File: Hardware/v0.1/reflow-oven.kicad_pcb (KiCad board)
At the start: 2 copper layers, 43 x 72 mm, 2 parts, among them U1 WeAct_MiniF4

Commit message: Finished schematics
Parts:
- added BZ1: HNB09A03, _AKL_Speaker:HNB09A03, B.Cu at (11.2, -23.0)
- added C1: 100n, Capacitor_SMD:C_0603_1608Metric, B.Cu at (0.10, -23.3)
- added C2: 10n, Capacitor_SMD:C_0603_1608Metric, B.Cu at (0.10, -25.8)
- added D1: MBR120VLSFT3G, _AKL_Diode:SOD-123FL, F.Cu at (-3.10, -63.0)
- added D2: MBR120VLSFT3G, _AKL_Diode:SOD-123FL, F.Cu at (-3.10, -59.9)
- added FB1: Ferrite_Bead, Inductor_SMD:L_0603_1608Metric, B.Cu at (4.11, -23.3)
- added FB2: Ferrite_Bead, Inductor_SMD:L_0603_1608Metric, B.Cu at (4.11, -25.8)
- added J1: WJ124-3.81-2P, _AKL_Connector:WJ124-3.81-2P, B.Cu at (-14.9, -22.6)
- added J2: WJ124-3.81-2P, _AKL_Connector:WJ124-3.81-2P, B.Cu at (-14.9, -15.0)
- added J3: WJ124-3.81-2P, _AKL_Connector:WJ124-3.81-2P, B.Cu at (-14.9, -7.37)
- added J4: WJ124-3.81-2P, _AKL_Connector:WJ124-3.81-2P, B.Cu at (-14.9, 0.25)
- added Q1: FDN327N, Package_TO_SOT_SMD:SOT-23, F.Cu at (1.94, -62.2)
- added Q2: FDN327N, Package_TO_SOT_SMD:SOT-23, F.Cu at (1.94, -57.7)
- added R1: 10K, Resistor_SMD:R_0603_1608Metric, F.Cu at (-3.96, -57.2)
- added R2: 10K, Resistor_SMD:R_0603_1608Metric, F.Cu at (6.17, -63.3)
- added R3: 10K, Resistor_SMD:R_0603_1608Metric, F.Cu at (6.17, -60.7)
- added R4: 10K, Resistor_SMD:R_0603_1608Metric, F.Cu at (6.17, -58.2)
- added R5: 10K, Resistor_SMD:R_0603_1608Metric, F.Cu at (6.17, -55.7)
- added SW1: TS-1095-A13B3-D1, Button_Switch_THT:SW_PUSH_6mm_H9.5mm, F.Cu at (-15.0, 34.0)
- added SW2: TS-1095-A13B3-D1, Button_Switch_THT:SW_PUSH_6mm_H9.5mm, F.Cu at (-2.25, 34.0)
- added SW3: TS-1095-A13B3-D1, Button_Switch_THT:SW_PUSH_6mm_H9.5mm, F.Cu at (10.5, 34.0)
- added U2: MAX31855KASA+T, Package_SO:SOIC-8_3.9x4.9mm_P1.27mm, B.Cu at (-6.77, -23.5)
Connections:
- DS1 pad 1: Net-(DS1-Pad1) -> /BL
- DS1 pad 2: Net-(DS1-Pad2) -> /RST
- DS1 pad 3: Net-(DS1-Pad3) -> /DC
- DS1 pad 4: Net-(DS1-Pad4) -> /CS1
- DS1 pad 5: Net-(DS1-Pad5) -> /SCK1
- DS1 pad 6: Net-(DS1-Pad6) -> /MOSI1
- DS1 pad 7: Net-(DS1-Pad7) -> GND
- DS1 pad 8: Net-(DS1-Pad8) -> /3V3
- U1 pad 1: Net-(U1-Pad1) -> /CS2
- U1 pad 10: Net-(U1-Pad10) -> (no net)
- U1 pad 11: Net-(U1-Pad11) -> (no net)
- U1 pad 12: Net-(U1-Pad12) -> (no net)
- U1 pad 13: Net-(U1-Pad13) -> /OUT1
- U1 pad 14: Net-(U1-Pad14) -> /OUT2
- U1 pad 15: Net-(U1-Pad15) -> (no net)
- U1 pad 16: Net-(U1-Pad16) -> (no net)
- U1 pad 17: Net-(U1-Pad17) -> (no net)
- U1 pad 18: Net-(U1-Pad18) -> /5V
- U1 pad 19: Net-(U1-Pad19) -> GND
- U1 pad 2: Net-(U1-Pad2) -> /SCK2
- U1 pad 20: Net-(U1-Pad20) -> /3V3
- U1 pad 21: Net-(U1-Pad21) -> (no net)
- U1 pad 22: Net-(U1-Pad22) -> (no net)
- U1 pad 23: Net-(U1-Pad23) -> (no net)
- U1 pad 24: Net-(U1-Pad24) -> (no net)
- U1 pad 25: Net-(U1-Pad25) -> (no net)
- U1 pad 26: Net-(U1-Pad26) -> (no net)
- U1 pad 27: Net-(U1-Pad27) -> /BUZZER
- U1 pad 28: Net-(U1-Pad28) -> /DC
- U1 pad 29: Net-(U1-Pad29) -> /RST
- U1 pad 3: Net-(U1-Pad3) -> /MISO2
- U1 pad 30: Net-(U1-Pad30) -> /CS1
- U1 pad 31: Net-(U1-Pad31) -> /SCK1
- U1 pad 32: Net-(U1-Pad32) -> /BL
- U1 pad 33: Net-(U1-Pad33) -> /MOSI1
- U1 pad 34: Net-(U1-Pad34) -> /BTN_C
- U1 pad 35: Net-(U1-Pad35) -> /BTN_B
- U1 pad 36: Net-(U1-Pad36) -> (no net)
- U1 pad 37: Net-(U1-Pad37) -> /BTN_A
- U1 pad 38: Net-(U1-Pad38) -> /3V3
- U1 pad 39: Net-(U1-Pad39) -> GND
- U1 pad 4: Net-(U1-Pad4) -> (no net)
- U1 pad 40: Net-(U1-Pad40) -> /5V
- U1 pad 5: Net-(U1-Pad5) -> (no net)
- U1 pad 6: Net-(U1-Pad6) -> (no net)
- U1 pad 7: Net-(U1-Pad7) -> (no net)
- U1 pad 8: Net-(U1-Pad8) -> (no net)
- U1 pad 9: Net-(U1-Pad9) -> (no net)

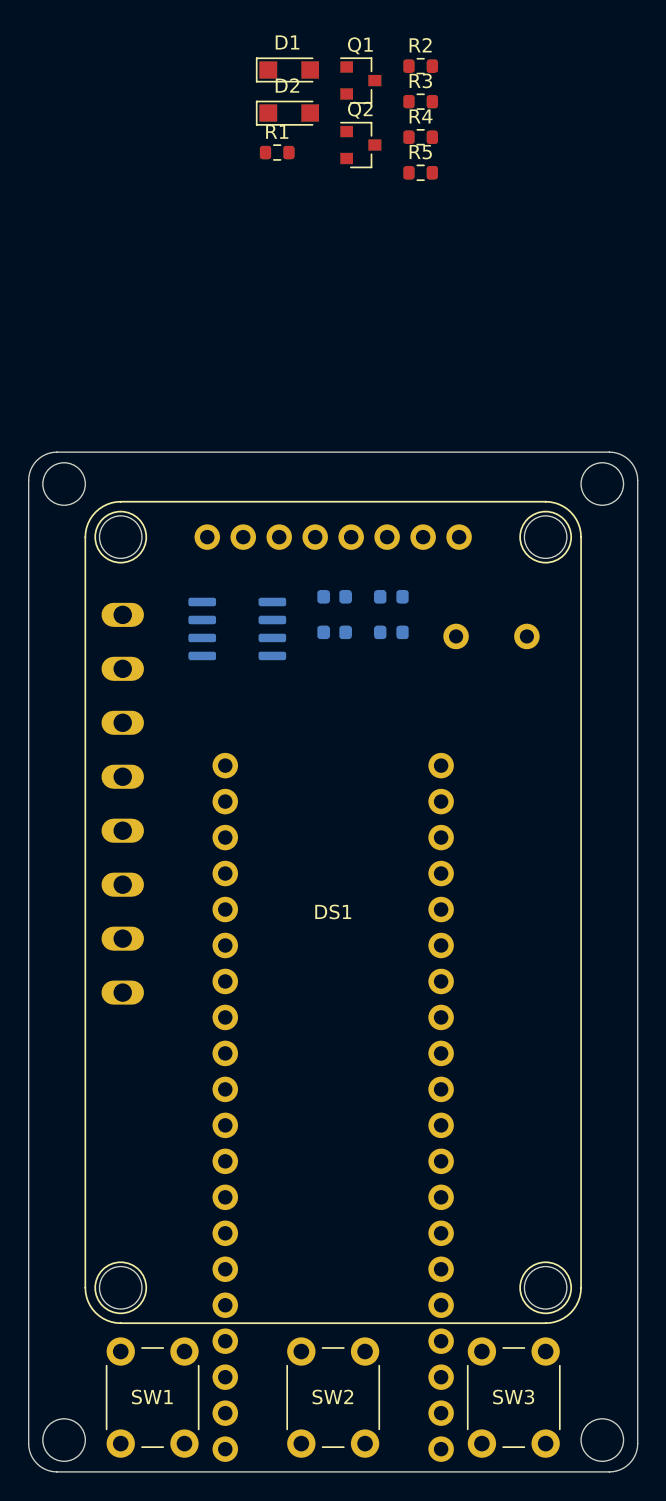
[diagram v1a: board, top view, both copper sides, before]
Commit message: Finished PCB layout
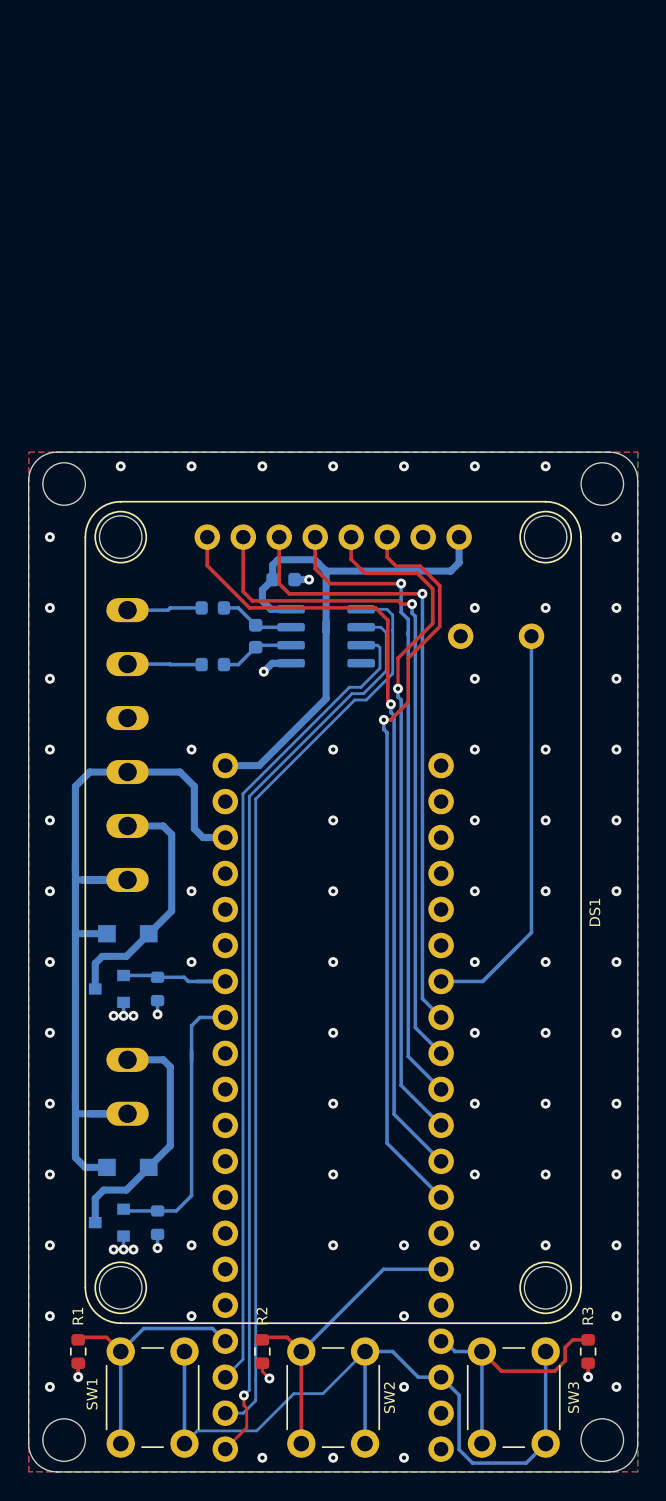
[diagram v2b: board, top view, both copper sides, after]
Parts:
- added REF**: OSHW-Logo_5.7x6mm_SilkScreen, Symbol:OSHW-Logo_5.7x6mm_SilkScreen, B.Cu at (15.5, -10.0)
- D1, D2, Q1, Q2, R4, R5: moved to B.Cu
- moved R2 91.4 mm to (-5.00, 27.5), turned to 270 degrees
- moved R3 89.0 mm to (18.0, 27.5), turned to 270 degrees
- moved R1 85.8 mm to (-18.0, 27.5), turned to 270 degrees
- moved Q2 78.1 mm to (-15.8, 18.4), turned to 180 degrees
- moved R5 76.4 mm to (-12.4, 18.4), turned to 270 degrees
- moved D2 75.3 mm to (-14.5, 14.5)
- moved Q1 66.5 mm to (-15.8, 1.90), turned to 180 degrees
- moved R4 62.9 mm to (-12.4, 1.90), turned to 270 degrees
- moved D1 62.0 mm to (-14.5, -2.00)
- moved FB2 13.5 mm to (-8.50, -21.0)
- moved FB1 12.7 mm to (-8.50, -25.0)
- moved J4 8.56 mm to (-14.5, 8.81)
- moved J2 7.96 mm to (-14.5, -22.9)
- moved J1 7.29 mm to (-14.5, -15.3)
- moved U2 6.29 mm to (-0.50, -23.0), turned to 0 degrees
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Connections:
- C1 pad 1: /3V3 -> /3V3_2
- DS1 pad 8: /3V3 -> /3V3_2
- J2 pad 1: /T+ -> /T-
- J2 pad 2: /T- -> /T+
- U1 pad 13: /OUT1 -> /OUT2
- U1 pad 14: /OUT2 -> /OUT1
- U1 pad 20: /3V3 -> /3V3_2
- U1 pad 34: /BTN_C -> (no net)
- U1 pad 37: /BTN_A -> /BTN_C
- U1 pad 4: (no net) -> /BTN_A
- U1 pad 40: /5V -> (no net)
- U2 pad 4: /3V3 -> /3V3_2
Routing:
- net /SCK2: track 0.00 -> 65.6 mm
- net /CS2: track 0.00 -> 64.9 mm, vias 0 -> 1
- net /5V: track 0.00 -> 60.2 mm
- net /MISO2: track 0.00 -> 57.9 mm
- net /BL: track 0.00 -> 56.1 mm, vias 0 -> 1
- net /3V3: track 0.00 -> 53.8 mm
- net /MOSI1: track 0.00 -> 52.7 mm, vias 0 -> 1
- net /RST: track 0.00 -> 48.7 mm, vias 0 -> 1
- net /SCK1: track 0.00 -> 48.3 mm, vias 0 -> 1
- net /CS1: track 0.00 -> 45.8 mm, vias 0 -> 1
- net /DC: track 0.00 -> 44.2 mm, vias 0 -> 1
- net /3V3_2: track 0.00 -> 39.6 mm
- net /BUZZER: track 0.00 -> 32.2 mm
- net /BTN_B: track 0.00 -> 22.2 mm
- net /OUT2: track 0.00 -> 20.8 mm
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- added copper zone on B.Cu, net GND
- added copper zone on F.Cu, net GND
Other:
- net class Default: clearance 0.2 -> 0.25; via_dia 0.8 -> 0.7; via_drill 0.4 -> 0.3
- net class Power added: clearance 0.25, trace_width 0.5, via_dia 0.7, via_drill 0.3
- rule trace_clearance: 0.2 -> 0.25
- rule via_min_size: 0.4 -> 0.7
- board text added: "5V"
- board text added: "GND"
- board text added: "REFLOW OVEN CONTROLLER"
- board text added: "S1+"
- board text added: "S1-"
- board text added: "S2+"
- board text added: "S2-"
- board text added: "T+"
- board text added: "T-"
- board text added: "alfonsoluna.io"
- board text added: "v0.1 2020/12"
